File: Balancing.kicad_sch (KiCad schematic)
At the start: 1 part, among them U1 MP2790DFP-0002-T

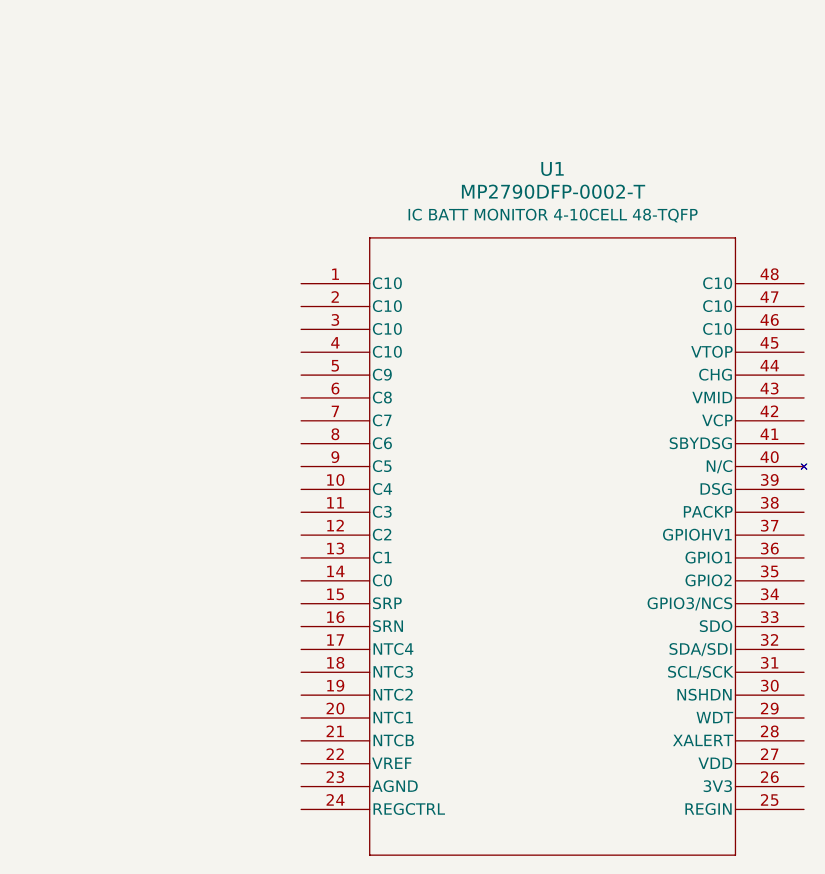
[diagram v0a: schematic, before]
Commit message: added hierarchy
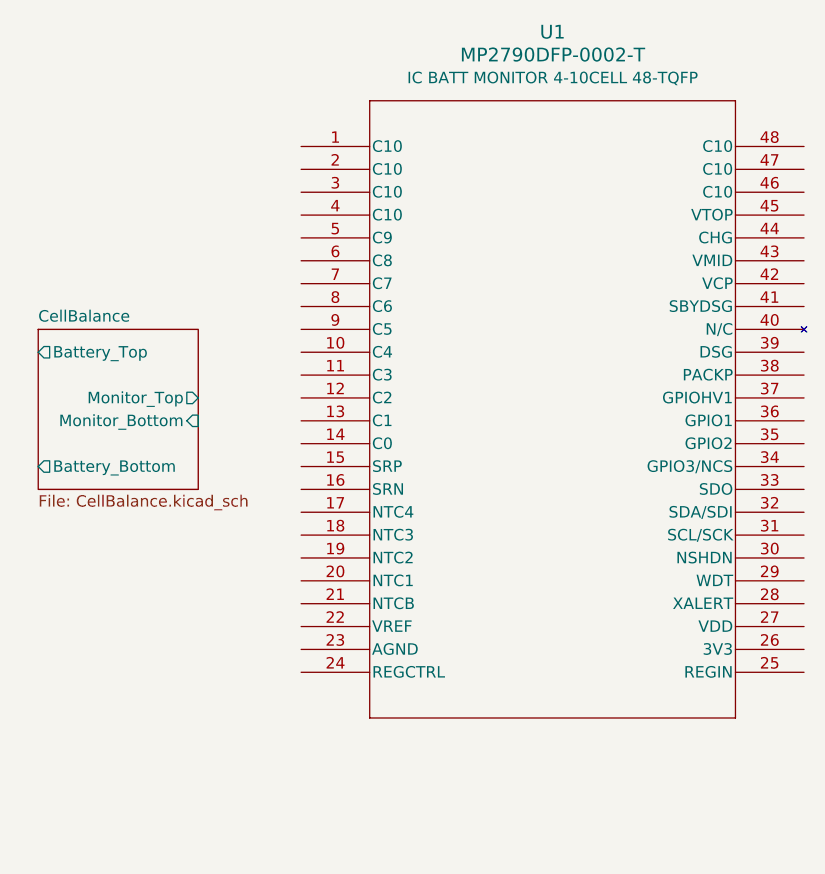
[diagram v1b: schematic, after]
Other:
- added sheet CellBalance (CellBalance.kicad_sch)
- moved on the sheet: U1
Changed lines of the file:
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@@
 	(symbol
 		(lib_id "symbols:MP2790DFP-0002-T")
-		(at 181.61 60.96 0)
+		(at 181.61 45.72 0)
 		(unit 1)
 		(body_style 1)
@@
 		(fields_autoplaced yes)
 		(property "Reference" "U1"
-			(at 209.55 48.26 0)
+			(at 209.55 33.02 0)
 			(show_name no)
 			(do_not_autoplace no)
@@
 		)
 		(property "Value" "MP2790DFP-0002-T"
-			(at 209.55 50.8 0)
+			(at 209.55 35.56 0)
 			(show_name no)
 			(do_not_autoplace no)
@@
 		)
 		(property "Footprint" "footprints:TQFP-48_MP2790_MNP"
-			(at 181.61 60.96 0)
+			(at 181.61 45.72 0)
 			(hide yes)
 			(show_name no)
@@
 		)
 		(property "Datasheet" "https://www.digikey.ca/en/products/detail/monolithic-power-systems-inc/MP2790DFP-0002-T/22589381"
-			(at 181.61 60.96 0)
+			(at 181.61 45.72 0)
 			(hide yes)
 			(show_name no)
@@
 		)
 		(property "Description" "IC BATT MONITOR 4-10CELL 48-TQFP"
-			(at 209.55 53.34 0)
+			(at 209.55 38.1 0)
 			(show_name no)
 			(do_not_autoplace no)
@@
 				)
 			)
+		)
+	)
+	(sheet
+		(at 152.4 66.04)
+		(size 17.78 17.78)
+		(exclude_from_sim no)
+		(in_bom yes)
+		(on_board yes)
+		(dnp no)
+		(fields_autoplaced yes)
+		(stroke
+			(width 0.1524)
+			(type solid)
+		)
+		(fill
+			(color 0 0 0 0)
+		)
+		(property "Sheetname" "CellBalance"
+			(at 152.4 65.3284 0)
+			(show_name no)
+			(do_not_autoplace no)
+			(effects
+				(font
+					(size 1.27 1.27)
+				)
+				(justify left bottom)
+			)
+		)
+		(property "Sheetfile" "CellBalance.kicad_sch"
+			(at 152.4 84.4046 0)
+			(show_name no)
+			(do_not_autoplace no)
+			(effects
+				(font
+					(size 1.27 1.27)
+				)
+				(justify left top)
+			)
+		)
+		(pin "Battery_Bottom" output
+			(at 152.4 81.28 180)
+			(effects
+				(font
+					(size 1.27 1.27)
+				)
+				(justify left)
+			)
+		)
+		(pin "Monitor_Bottom" input
+			(at 170.18 76.2 0)
+			(effects
+				(font
+					(size 1.27 1.27)
+				)
+				(justify right)
+			)
+		)
+		(pin "Battery_Top" output
+			(at 152.4 68.58 180)
+			(effects
+				(font
+					(size 1.27 1.27)
+				)
+				(justify left)
+			)
+		)
+		(pin "Monitor_Top" output
+			(at 170.18 73.66 0)
+			(effects
+				(font
+					(size 1.27 1.27)
+				)
+				(justify right)
+			)
+		)
+		(instances
+			(project "bms-afe"
+				(path "/226a23e7-09bb-40bc-b53a-ec42a6b7cc90/9aa16ca4-990b-4c84-ac14-7f5aa42928e6"
+					(page "4")
+				)
+			)

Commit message: mostly done afe ic
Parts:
- removed U1: MP2790DFP-0002-T, footprints:TQFP-48_MP2790_MNP, symbol symbols:MP2790DFP-0002-T
- added U1: TLE9012DQUXUMA1, footprints:PG-TQFP-48-9, symbol symbols:TLE9012DQUXUMA1

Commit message: schematic done except for pulse transformer
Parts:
- removed U1: TLE9012DQUXUMA1, footprints:PG-TQFP-48-9, symbol symbols:TLE9012DQUXUMA1
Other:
- removed sheet CellBalance
